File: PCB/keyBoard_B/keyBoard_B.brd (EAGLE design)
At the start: 169.5 x 134.6 mm, 286 parts

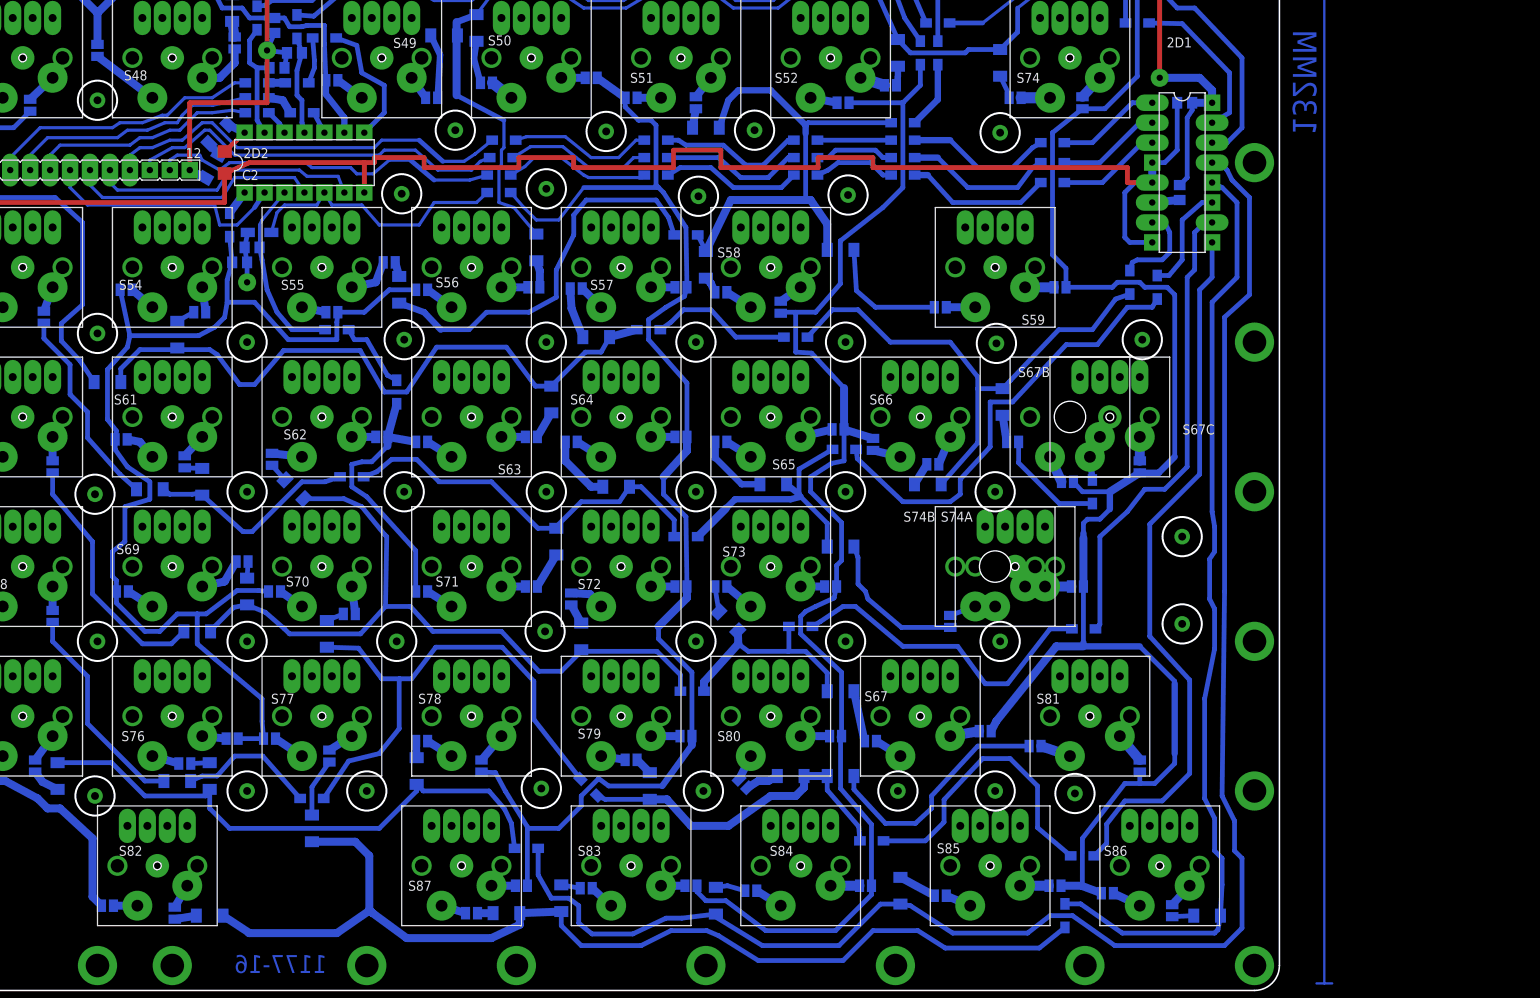
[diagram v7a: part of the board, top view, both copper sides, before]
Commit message: add kesize table. bad pcb a b
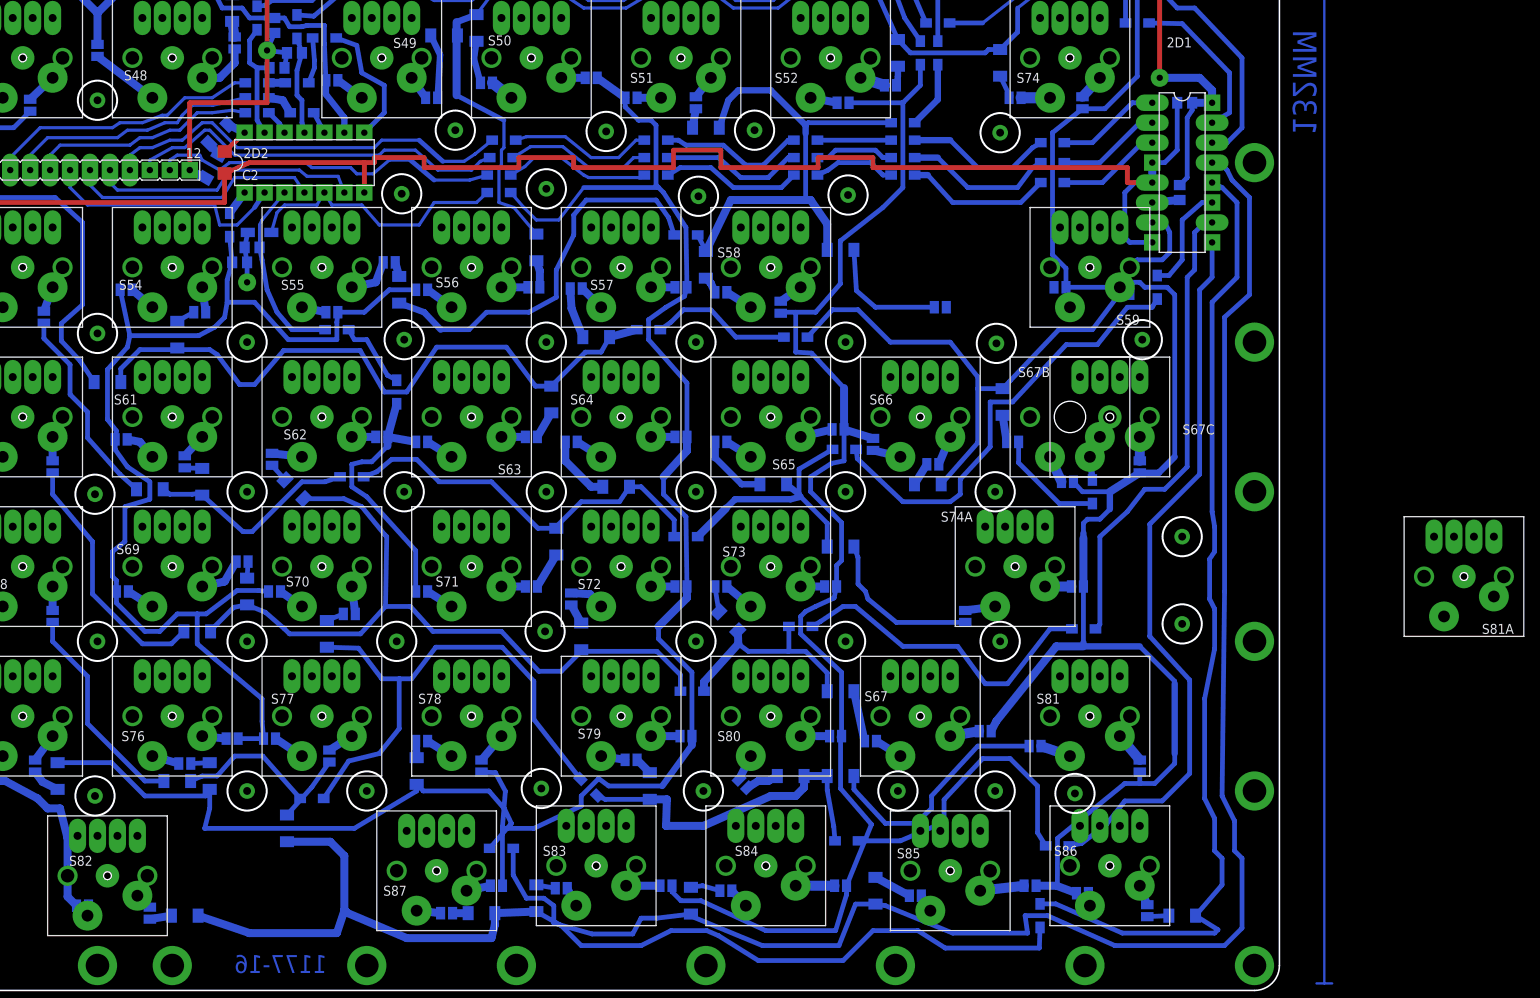
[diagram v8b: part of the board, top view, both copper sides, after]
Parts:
- removed S74B: Enter, cherrymx:CHERRY-MX
- added S81A: R Shift, cherrymx:CHERRY-MX-4P
- added U$4, U$5, U$7: (no value), kbmx:18X18
- added U$6: (no value), kbmx:18X23
- added U$8: (no value), kbmx:18X42
- moved U$80 27.7 mm to (150.2, 129.9)
- moved U$79 22.1 mm to (28.9, 6.03)
- moved S59 12.1 mm to (154.6, 103.2)
- moved S82 6.48 mm to (29.5, 25.7)
- moved U$84 6.35 mm to (135.6, 27.0)
- moved U$85 6.35 mm to (111.4, 27.0)
- moved U$90 6.35 mm to (88.6, 28.3)
- moved S86 6.35 mm to (157.2, 27.0)
- moved U$83 6.35 mm to (155.9, 28.3)
- moved U$86 6.35 mm to (68.3, 27.0)
- moved S85 5.12 mm to (136.8, 26.4)
- moved S83 4.45 mm to (91.8, 27.0)
- moved S84 4.45 mm to (113.3, 27.0)
- moved J52 3.42 mm to (150.5, 29.5)
- moved S87 3.24 mm to (71.4, 26.4)
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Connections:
- net N$186: now also S81A.SW2
- net N$263: now also S81A.SW1
- net N$94: no longer S74B.SW1
- net N$97: no longer S74B.SW2
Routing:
- net 7: track 208.9 -> 214.6 mm
- net 8: track 120.1 -> 125.7 mm
- net N$183: track 3.68 -> 0.00 mm
- net N$265: track 3.68 -> 0.00 mm
- net 7J: track 72.1 -> 74.6 mm
- net N$94: track 5.91 -> 3.37 mm
- net G6: track 214.1 -> 216.4 mm
- net N$29: track 3.72 -> 1.60 mm
- net N$97: track 5.91 -> 3.84 mm
- net N$251: track 3.68 -> 5.62 mm
- net G4: track 167.5 -> 169.4 mm
- net N$233: track 3.05 -> 1.28 mm
- net 8J: track 134.9 -> 136.6 mm
- net G1: track 198.1 -> 196.4 mm
- net G5: track 167.9 -> 169.5 mm
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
